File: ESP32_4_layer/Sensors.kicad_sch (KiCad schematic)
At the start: 17 parts, among them Q1 TEMT6000X01, U6 BME280, U7 MAX4466EXK

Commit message: hierarchial label attached
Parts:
- C17, C18, C19, C20: footprint (none) -> Capacitor_SMD:C_0805_2012Metric
- R21, R22, R23, R24, R25, R26, R27, R28, R29: footprint (none) -> Resistor_SMD:R_0805_2012Metric
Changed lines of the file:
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@@
 			)
 		)
-		(property "Footprint" ""
+		(property "Footprint" "Resistor_SMD:R_0805_2012Metric"
 			(at 96.52 75.438 90)
 			(effects
@@
 			)
 		)
-		(property "Footprint" ""
+		(property "Footprint" "Resistor_SMD:R_0805_2012Metric"
 			(at 73.66 123.698 90)
 			(effects
@@
 			)
 		)
-		(property "Footprint" ""
+		(property "Footprint" "Resistor_SMD:R_0805_2012Metric"
 			(at 170.942 67.31 90)
 			(effects
@@
 			)
 		)
-		(property "Footprint" ""
+		(property "Footprint" "Resistor_SMD:R_0805_2012Metric"
 			(at 170.942 74.93 90)
 			(effects
@@
 			)
 		)
-		(property "Footprint" ""
+		(property "Footprint" "Resistor_SMD:R_0805_2012Metric"
 			(at 96.52 70.358 90)
 			(effects
@@
 			)
 		)
-		(property "Footprint" ""
+		(property "Footprint" "Capacitor_SMD:C_0805_2012Metric"
 			(at 168.91 70.1548 0)
 			(effects
@@
 			)
 		)
-		(property "Footprint" ""
+		(property "Footprint" "Resistor_SMD:R_0805_2012Metric"
 			(at 214.63 103.378 90)
 			(effects
@@
 			)
 		)
-		(property "Footprint" ""
+		(property "Footprint" "Capacitor_SMD:C_0805_2012Metric"
 			(at 218.44 105.7148 0)
 			(effects
@@
 			)
 		)
-		(property "Footprint" ""
+		(property "Footprint" "Resistor_SMD:R_0805_2012Metric"
 			(at 187.452 92.71 90)
 			(effects
@@
 			)
 		)
-		(property "Footprint" ""
+		(property "Footprint" "Resistor_SMD:R_0805_2012Metric"
 			(at 179.832 76.2 90)
 			(effects
@@
 			)
 		)
-		(property "Footprint" ""
+		(property "Footprint" "Capacitor_SMD:C_0805_2012Metric"
 			(at 247.3452 85.09 0)
 			(effects
@@
 			)
 		)
-		(property "Footprint" ""
+		(property "Footprint" "Resistor_SMD:R_0805_2012Metric"
 			(at 179.832 92.71 90)
 			(effects
@@
 			)
 		)
-		(property "Footprint" ""
+		(property "Footprint" "Capacitor_SMD:C_0805_2012Metric"
 			(at 55.5752 60.96 0)
 			(effects

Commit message: PCB Stack up, netlist and constrainsts applied
Signed-off-by: jayaraj <jayarajemengineer@gmail.com>
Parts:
- MK1: footprint CMC-5042PF-AC:CUI_CMC-5042PF-AC -> Own_Library:CUI_CMC-5042PF-AC
- Q1: footprint TEMT6000X01:TRANS_TEMT6000X01 -> Own_Library:TEMT6000X01
- R21, R22: value 4.7k -> 4k7
- R23: value 4.7k -> 10k
- U7: footprint MAX4466EXK:SOT65P210X110-5N -> Own_Library:MAX4466EXX
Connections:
- net PHOTO_C: now reaches Q1.3, R23.1
- net SDA: now reaches R22.1, U6.3 (SDI)
- net SCL: now reaches R21.1, U6.4 (SCK)
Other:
- moved on the sheet: R23
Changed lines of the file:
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@@
+	)
+	(junction
+		(at 69.85 121.92)
+		(diameter 0)
+		(color 0 0 0 0)
 	)
 	(junction
@@
 	)
 	(junction
-		(at 104.14 73.66)
+		(at 87.63 68.58)
 		(diameter 0)
 		(color 0 0 0 0)
@@
 	)
 	(junction
+		(at 104.14 68.58)
+		(diameter 0)
+		(color 0 0 0 0)
+	)
+	(junction
+		(at 87.63 73.66)
+		(diameter 0)
+		(color 0 0 0 0)
+	)
+	(junction
 		(at 196.85 85.09)
 		(diameter 0)
@@
 	)
 	(junction
+		(at 104.14 73.66)
+		(diameter 0)
+		(color 0 0 0 0)
+	)
+	(junction
 		(at 181.61 101.6)
 		(diameter 0)
@@
 	)
 	(junction
-		(at 104.14 68.58)
-		(diameter 0)
-		(color 0 0 0 0)
-	)
-	(junction
 		(at 181.61 60.96)
 		(diameter 0)
@@
 	(wire
 		(pts
-			(xy 92.71 68.58) (xy 86.36 68.58)
+			(xy 69.85 121.92) (xy 66.04 121.92)
 		)
 		(stroke
@@
 	(wire
 		(pts
+			(xy 87.63 73.66) (xy 92.71 73.66)
+		)
+		(stroke
+			(width 0)
+			(type default)
+		)
+	)
+	(wire
+		(pts
 			(xy 54.61 53.34) (xy 68.58 53.34)
 		)
@@
 	(wire
 		(pts
-			(xy 69.85 121.92) (xy 66.04 121.92)
+			(xy 87.63 68.58) (xy 92.71 68.58)
+		)
+		(stroke
+			(width 0)
+			(type default)
+		)
+	)
+	(wire
+		(pts
+			(xy 74.93 121.92) (xy 69.85 121.92)
 		)
 		(stroke
@@
 	(wire
 		(pts
+			(xy 86.36 68.58) (xy 87.63 68.58)
+		)
+		(stroke
+			(width 0)
+			(type default)
+		)
+	)
+	(wire
+		(pts
+			(xy 69.85 121.92) (xy 69.85 125.73)
+		)
+		(stroke
+			(width 0)
+			(type default)
+		)
+	)
+	(wire
+		(pts
+			(xy 87.63 68.58) (xy 87.63 69.85)
+		)
+		(stroke
+			(width 0)
+			(type default)
+		)
+	)
+	(wire
+		(pts
 			(xy 196.85 85.09) (xy 196.85 101.6)
 		)
@@
 	(wire
 		(pts
+			(xy 87.63 63.5) (xy 86.36 63.5)
+		)
+		(stroke
+			(width 0)
+			(type default)
+		)
+	)
+	(wire
+		(pts
 			(xy 181.61 82.55) (xy 181.61 88.9)
 		)
@@
 	(wire
 		(pts
-			(xy 87.63 63.5) (xy 86.36 63.5)
-		)
-		(stroke
-			(width 0)
-			(type default)
-		)
-	)
-	(wire
-		(pts
 			(xy 189.23 96.52) (xy 189.23 101.6)
 		)
@@
 	(wire
 		(pts
+			(xy 87.63 76.2) (xy 87.63 73.66)
+		)
+		(stroke
+			(width 0)
+			(type default)
+		)
+	)
+	(wire
+		(pts
 			(xy 218.44 106.68) (xy 223.52 106.68)
 		)
@@
 	(wire
 		(pts
+			(xy 87.63 73.66) (xy 86.36 73.66)
+		)
+		(stroke
+			(width 0)
+			(type default)
+		)
+	)
+	(wire
+		(pts
 			(xy 100.33 73.66) (xy 104.14 73.66)
 		)
@@
 	(wire
 		(pts
-			(xy 92.71 73.66) (xy 86.36 73.66)
-		)
-		(stroke
-			(width 0)
-			(type default)
-		)
-	)
-	(wire
-		(pts
-			(xy 85.09 121.92) (xy 77.47 121.92)
+			(xy 85.09 121.92) (xy 82.55 121.92)
 		)
 		(stroke
@@
 	(wire
 		(pts
+			(xy 104.14 68.58) (xy 104.14 73.66)
+		)
+		(stroke
+			(width 0)
+			(type default)
+		)
+	)
+	(wire
+		(pts
 			(xy 68.58 55.88) (xy 68.58 53.34)
 		)
@@
 	(wire
 		(pts
-			(xy 104.14 68.58) (xy 104.14 73.66)
-		)
-		(stroke
-			(width 0)
-			(type default)
-		)
-	)
-	(wire
-		(pts
 			(xy 181.61 58.42) (xy 181.61 60.96)
 		)
@@
 		)
 	)
-	(hierarchical_label "SCL"
-		(shape input)
-		(at 104.14 68.58 0)
+	(hierarchical_label "PHOTO_C"
+		(shape output)
+		(at 69.85 125.73 0)
 		(effects
 			(font
 				(size 1.27 1.27)
+				(thickness 0.254)
+				(bold yes)
 			)
 			(justify left)
@@
 		)
 	)
-	(hierarchical_label "PHOTO_C"
-		(shape output)
-		(at 85.09 121.92 0)
-		(effects
-			(font
-				(size 1.27 1.27)
-				(thickness 0.254)
-				(bold yes)
-			)
-			(justify left)
-		)
-	)
 	(hierarchical_label "MIC_OUT"
 		(shape output)
@@
 	(hierarchical_label "SDA"
 		(shape input)
-		(at 104.14 73.66 0)
+		(at 87.63 76.2 0)
+		(effects
+			(font
+				(size 1.27 1.27)
+			)
+			(justify left)
+		)
+	)
+	(hierarchical_label "SCL"
+		(shape input)
+		(at 87.63 69.85 0)
 		(effects
 			(font
@@
 			)
 		)
-		(property "Footprint" "TEMT6000X01:TRANS_TEMT6000X01"
+		(property "Footprint" "Own_Library:TEMT6000X01"
 			(at 60.96 119.38 0)
 			(effects
@@
 			)
 		)
-		(property "Value" "4.7k"
+		(property "Value" "4k7"
 			(at 101.854 72.39 90)
 			(effects
@@
 	(symbol
 		(lib_id "Device:R")
-		(at 73.66 121.92 90)
+		(at 78.74 121.92 90)
 		(unit 1)
 		(exclude_from_sim no)
@@
 		(dnp no)
 		(property "Reference" "R23"
-			(at 68.834 120.396 90)
-			(effects
-				(font
-					(size 1.27 1.27)
-				)
-			)
-		)
-		(property "Value" "4.7k"
-			(at 77.978 119.634 90)
+			(at 73.914 120.396 90)
+			(effects
+				(font
+					(size 1.27 1.27)
+				)
+			)
+		)
+		(property "Value" "10k"
+			(at 83.058 119.634 90)
 			(effects
 				(font
@@
 		)
 		(property "Footprint" "Resistor_SMD:R_0805_2012Metric"
-			(at 73.66 123.698 90)
+			(at 78.74 123.698 90)
 			(effects
 				(font
@@
 		)
 		(property "Datasheet" "~"
-			(at 73.66 121.92 0)
+			(at 78.74 121.92 0)
 			(effects
 				(font
@@
 		)
 		(property "Description" "Resistor"
-			(at 73.66 121.92 0)
+			(at 78.74 121.92 0)
 			(effects
 				(font
@@
 			)
 		)
-		(property "Value" "4.7k"
+		(property "Value" "4k7"
 			(at 100.838 66.294 90)
 			(effects
@@
 			)
 		)
-		(property "Footprint" "CMC-5042PF-AC:CUI_CMC-5042PF-AC"
+		(property "Footprint" "Own_Library:CUI_CMC-5042PF-AC"
 			(at 162.56 85.09 0)
 			(effects
@@
 			)
 		)
-		(property "Footprint" "MAX4466EXK:SOT65P210X110-5N"
+		(property "Footprint" "Own_Library:MAX4466EXX"
 			(at 214.63 85.09 0)
 			(effects

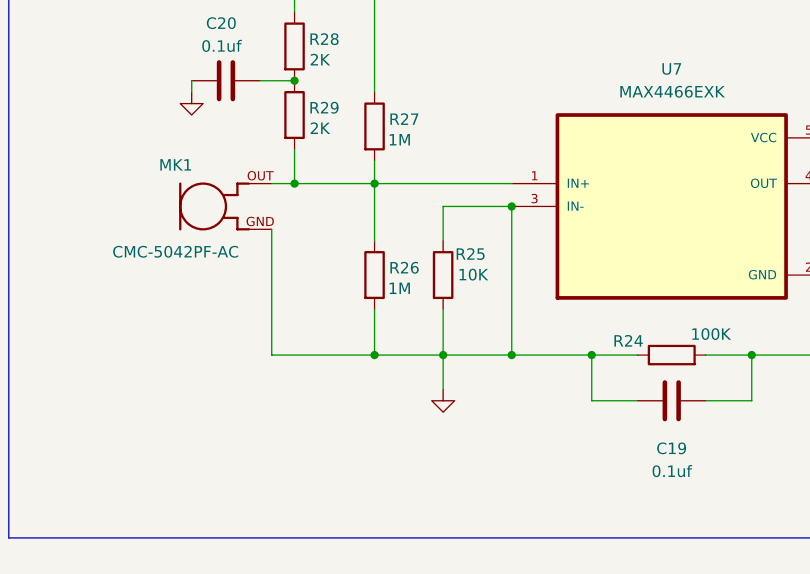
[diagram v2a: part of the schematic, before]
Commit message: upto inner layer copper zone
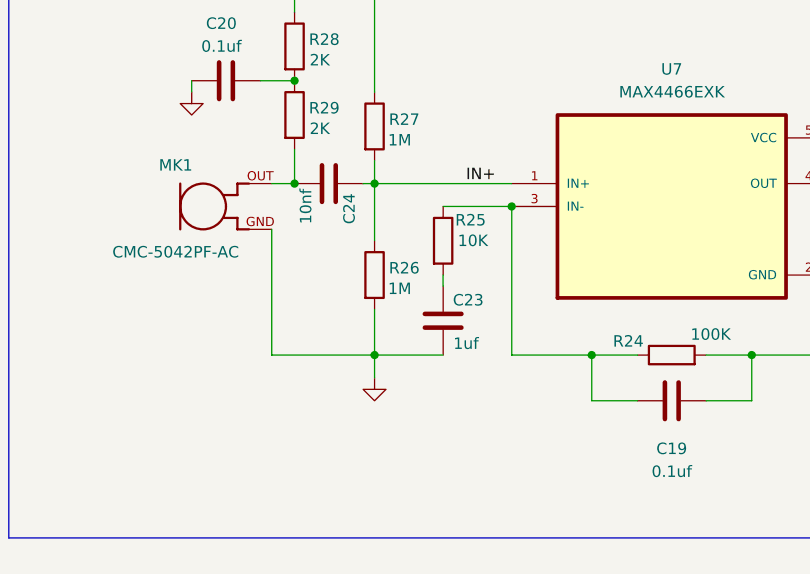
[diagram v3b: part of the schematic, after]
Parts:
- added C23: 1uf, Capacitor_SMD:C_0805_2012Metric, symbol Device:C
- added C24: 10nf, Capacitor_SMD:C_0805_2012Metric, symbol Device:C
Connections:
- net GND: now also C23.1; no longer C19.1, R24.1, R25.1, R25.2, U7.3 (IN-)
- net IN+: now reaches R26.1, R27.2, U7.1 (IN+)
- net IN+: now also C24.2; no longer MK1.OUT, R29.2
- new net: C23.2, R25.2
- new net: C24.1, MK1.OUT, R29.2
- new net: C19.1, R24.1, R25.1, U7.3 (IN-)
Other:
- moved on the sheet: R25
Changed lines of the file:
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@@
-	)
-	(junction
-		(at 196.85 101.6)
-		(diameter 0)
-		(color 0 0 0 0)
 	)
 	(junction
@@
 	)
 	(junction
-		(at 189.23 101.6)
-		(diameter 0)
-		(color 0 0 0 0)
-	)
-	(junction
 		(at 68.58 53.34)
 		(diameter 0)
@@
 	)
 	(junction
-		(at 172.72 82.55)
-		(diameter 0)
-		(color 0 0 0 0)
-	)
-	(junction
 		(at 223.52 101.6)
 		(diameter 0)
@@
 		(color 0 0 0 0)
 	)
+	(junction
+		(at 172.72 82.55)
+		(diameter 0)
+		(color 0 0 0 0)
+	)
 	(wire
 		(pts
@@
 	(wire
 		(pts
-			(xy 189.23 101.6) (xy 189.23 105.41)
-		)
-		(stroke
-			(width 0)
-			(type default)
-		)
-	)
-	(wire
-		(pts
-			(xy 196.85 101.6) (xy 189.23 101.6)
+			(xy 181.61 101.6) (xy 181.61 104.14)
 		)
 		(stroke
@@
 	(wire
 		(pts
-			(xy 189.23 88.9) (xy 189.23 85.09)
-		)
-		(stroke
-			(width 0)
-			(type default)
-		)
-	)
-	(wire
-		(pts
 			(xy 86.36 68.58) (xy 87.63 68.58)
 		)
@@
 	(wire
 		(pts
+			(xy 189.23 92.71) (xy 189.23 93.98)
+		)
+		(stroke
+			(width 0)
+			(type default)
+		)
+	)
+	(wire
+		(pts
 			(xy 196.85 85.09) (xy 196.85 101.6)
 		)
@@
 	(wire
 		(pts
-			(xy 172.72 82.55) (xy 181.61 82.55)
-		)
-		(stroke
-			(width 0)
-			(type default)
-		)
-	)
-	(wire
-		(pts
-			(xy 189.23 96.52) (xy 189.23 101.6)
-		)
-		(stroke
-			(width 0)
-			(type default)
-		)
-	)
-	(wire
-		(pts
 			(xy 87.63 76.2) (xy 87.63 73.66)
 		)
@@
 	(wire
 		(pts
+			(xy 181.61 101.6) (xy 189.23 101.6)
+		)
+		(stroke
+			(width 0)
+			(type default)
+		)
+	)
+	(wire
+		(pts
 			(xy 170.18 87.63) (xy 170.18 101.6)
 		)
@@
 	(wire
 		(pts
+			(xy 180.34 82.55) (xy 181.61 82.55)
+		)
+		(stroke
+			(width 0)
+			(type default)
+		)
+	)
+	(wire
+		(pts
 			(xy 223.52 106.68) (xy 223.52 101.6)
 		)
@@
 	(wire
 		(pts
-			(xy 181.61 101.6) (xy 189.23 101.6)
-		)
-		(stroke
-			(width 0)
-			(type default)
-		)
-	)
-	(wire
-		(pts
 			(xy 170.18 101.6) (xy 181.61 101.6)
 		)
@@
 			(width 0)
 			(type default)
+		)
+	)
+	(label "IN+"
+		(at 191.77 82.55 0)
+		(effects
+			(font
+				(size 1.27 1.27)
+			)
+			(justify left bottom)
 		)
 	)
@@
 	)
 	(symbol
+		(lib_id "Device:C")
+		(at 189.23 97.79 180)
+		(unit 1)
+		(exclude_from_sim no)
+		(in_bom yes)
+		(on_board yes)
+		(dnp no)
+		(property "Reference" "C23"
+			(at 192.024 95.504 0)
+			(effects
+				(font
+					(size 1.27 1.27)
+				)
+			)
+		)
+		(property "Value" "1uf"
+			(at 191.77 100.33 0)
+			(effects
+				(font
+					(size 1.27 1.27)
+				)
+			)
+		)
+		(property "Footprint" "Capacitor_SMD:C_0805_2012Metric"
+			(at 188.2648 93.98 0)
+			(effects
+				(font
+					(size 1.27 1.27)
+				)
+				(hide yes)
+			)
+		)
+		(property "Datasheet" "~"
+			(at 189.23 97.79 0)
+			(effects
+				(font
+					(size 1.27 1.27)
+				)
+				(hide yes)
+			)
+		)
+		(property "Description" "Unpolarized capacitor"
+			(at 189.23 97.79 0)
+			(effects
+				(font
+					(size 1.27 1.27)
+				)
+				(hide yes)
+			)
+		)
+		(pin "1"
+		)
+		(pin "2"
+		)
+		(instances
+			(project "ESP32_4_layer"
+				(path "/052df048-a7d0-4515-b7e6-6d4a36313ca3/8eb72682-883d-43eb-a283-0b8e7a8d42e7/f0ef0ead-4efc-45c3-b9e3-f77bcee4fcd0"
+					(reference "C23")
+					(unit 1)
+				)
+			)
+		)
+	)
+	(symbol
 		(lib_id "Own_Library:TEMT6000X01")
 		(at 60.96 119.38 270)
@@
 	(symbol
 		(lib_id "power:GND")
-		(at 189.23 105.41 0)
+		(at 181.61 104.14 0)
 		(unit 1)
 		(exclude_from_sim no)
@@
 		(fields_autoplaced yes)
 		(property "Reference" "#PWR046"
-			(at 189.23 111.76 0)
+			(at 181.61 110.49 0)
 			(effects
 				(font
@@
 		)
 		(property "Value" "GND"
-			(at 189.23 110.49 0)
+			(at 181.61 109.22 0)
 			(effects
 				(font
@@
 		)
 		(property "Footprint" ""
-			(at 189.23 105.41 0)
+			(at 181.61 104.14 0)
 			(effects
 				(font
@@
 		)
 		(property "Datasheet" ""
-			(at 189.23 105.41 0)
+			(at 181.61 104.14 0)
 			(effects
 				(font
@@
 		)
 		(property "Description" "Power symbol creates a global label with name \"GND\" , ground"
-			(at 189.23 105.41 0)
+			(at 181.61 104.14 0)
 			(effects
 				(font
@@
 	(symbol
 		(lib_id "Device:R")
-		(at 189.23 92.71 0)
+		(at 189.23 88.9 0)
 		(unit 1)
 		(exclude_from_sim no)
@@
 		(dnp no)
 		(property "Reference" "R25"
-			(at 192.278 90.424 0)
+			(at 192.278 86.614 0)
 			(effects
 				(font
@@
 		)
 		(property "Value" "10K"
-			(at 192.532 92.71 0)
+			(at 192.532 88.9 0)
 			(effects
 				(font
@@
 		)
 		(property "Footprint" "Resistor_SMD:R_0805_2012Metric"
-			(at 187.452 92.71 90)
+			(at 187.452 88.9 90)
 			(effects
 				(font
@@
 		)
 		(property "Datasheet" "~"
-			(at 189.23 92.71 0)
+			(at 189.23 88.9 0)
 			(effects
 				(font
@@
 		)
 		(property "Description" "Resistor"
-			(at 189.23 92.71 0)
+			(at 189.23 88.9 0)
 			(effects
 				(font
@@
 					(unit 1)
 				)
+			)
+		)
+	)
+	(symbol
+		(lib_id "Device:C")
+		(at 176.53 82.55 90)
+		(unit 1)
+		(exclude_from_sim no)
+		(in_bom yes)
+		(on_board yes)
+		(dnp no)
+		(property "Reference" "C24"
+			(at 178.816 85.344 0)
+			(effects
+				(font
+					(size 1.27 1.27)
+				)
+			)
+		)
+		(property "Value" "10nf"
+			(at 173.99 85.09 0)
+			(effects
+				(font
+					(size 1.27 1.27)
+				)
+			)
+		)
+		(property "Footprint" "Capacitor_SMD:C_0805_2012Metric"
+			(at 180.34 81.5848 0)
+			(effects
+				(font
+					(size 1.27 1.27)
+				)
+				(hide yes)
+			)
+		)
+		(property "Datasheet" "~"
+			(at 176.53 82.55 0)
+			(effects
+				(font
+					(size 1.27 1.27)
+				)
+				(hide yes)
+			)
+		)
+		(property "Description" "Unpolarized capacitor"
+			(at 176.53 82.55 0)
+			(effects
+				(font
+					(size 1.27 1.27)
+				)
+				(hide yes)
+			)
+		)
+		(pin "1"
+		)
+		(pin "2"
+		)
+		(instances
+			(project "ESP32_4_layer"
+				(path "/052df048-a7d0-4515-b7e6-6d4a36313ca3/8eb72682-883d-43eb-a283-0b8e7a8d42e7/f0ef0ead-4efc-45c3-b9e3-f77bcee4fcd0"
+					(reference "C24")
+					(unit 1)
+				)
